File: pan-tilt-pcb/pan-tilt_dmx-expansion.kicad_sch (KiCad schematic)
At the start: 3 parts, among them J11 Conn_01x08, J12 Conn_01x08, J13 Conn_01x05

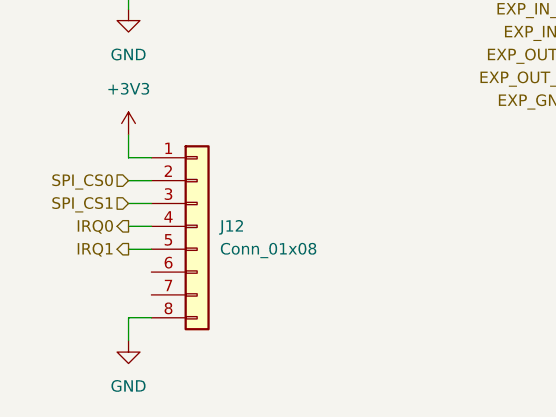
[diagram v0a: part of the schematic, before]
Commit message: fix missing pieces, incorporate review feedback
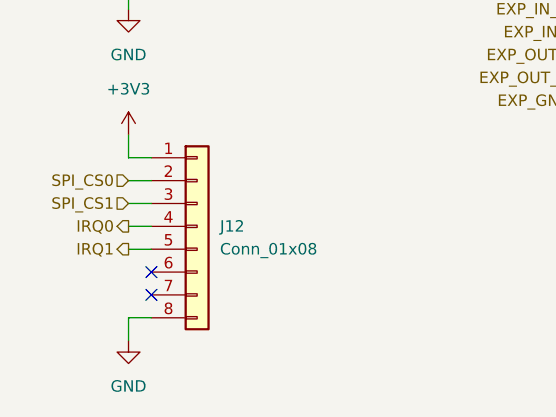
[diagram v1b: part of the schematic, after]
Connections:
- no-connect marks 0 -> 2
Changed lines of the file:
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@@
 		(comment 1 "Perry Naseck")
+	)
+	(no_connect
+		(at 124.46 116.84)
+	)
+	(no_connect
+		(at 124.46 119.38)
 	)
 	(wire
